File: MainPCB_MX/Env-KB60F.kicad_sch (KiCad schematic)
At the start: 157 parts, among them J1 TP3 Pad, J2 TP2 Pad, SW1 EVQ-P7A01P, U1 Pico

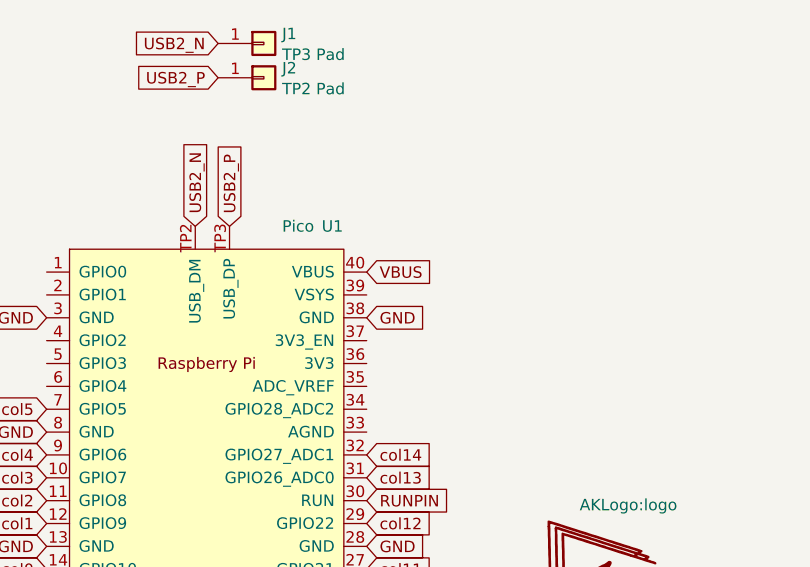
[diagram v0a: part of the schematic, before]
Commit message: swapped power input for MCU to VSYS instead of VBUS
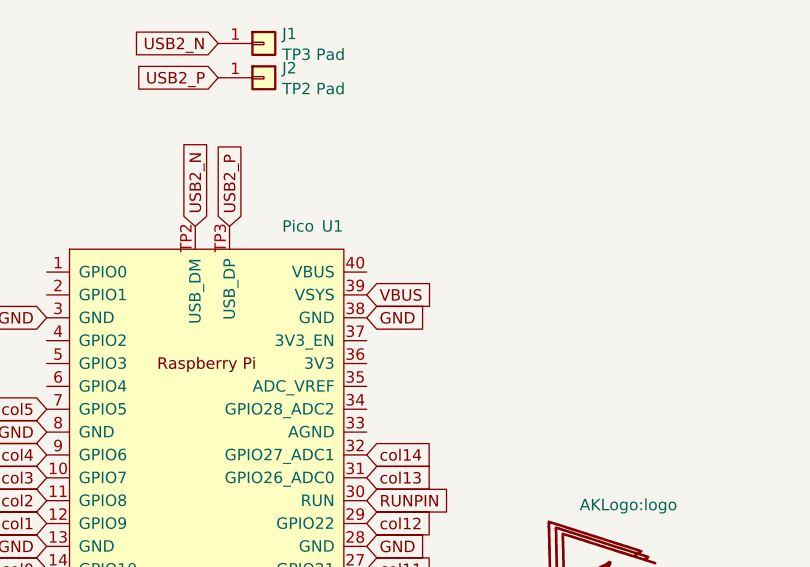
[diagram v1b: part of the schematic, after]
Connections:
- net VBUS: now also U1.39 (VSYS); no longer U1.40 (VBUS)
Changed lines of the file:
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@@
     )
   )
-  (global_label "VBUS" (shape input) (at 106.68 182.88 0) (fields_autoplaced)
+  (global_label "VBUS" (shape input) (at 106.68 185.42 0) (fields_autoplaced)
     (effects (font (size 1.27 1.27)) (justify left))
-    (property "Intersheet References" "${INTERSHEET_REFS}" (id 0) (at 0 0 0)
+    (property "Intersheet References" "${INTERSHEET_REFS}" (id 0) (at 0 2.54 0)
       (effects (font (size 1.27 1.27)) hide)
     )

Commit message: some various corrections to the USB DP/DM traces
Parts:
- U1: footprint MCU_RaspberryPi_and_Boards:RPi_Pico_SMD_TH -> MCU_RaspberryPi_and_Boards:RPi_Pico_SMD_TH_MODIFIED
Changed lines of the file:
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@@
     (property "Reference" "U1" (id 0) (at 102.87 177.8 0))
     (property "Value" "Pico" (id 1) (at 99.06 177.8 0))
-    (property "Footprint" "MCU_RaspberryPi_and_Boards:RPi_Pico_SMD_TH" (id 2) (at 88.9 207.01 90)
+    (property "Footprint" "MCU_RaspberryPi_and_Boards:RPi_Pico_SMD_TH_MODIFIED" (id 2) (at 88.9 207.01 90)
       (effects (font (size 1.27 1.27)) hide)
     )
@@
     )
     (path "/00000000-0000-0000-0000-00006095eae7"
-      (reference "U1") (unit 1) (value "Pico") (footprint "MCU_RaspberryPi_and_Boards:RPi_Pico_SMD_TH")
+      (reference "U1") (unit 1) (value "Pico") (footprint "MCU_RaspberryPi_and_Boards:RPi_Pico_SMD_TH_MODIFIED")
     )
     (path "/00000000-0000-0000-0000-000060a58fc0"
